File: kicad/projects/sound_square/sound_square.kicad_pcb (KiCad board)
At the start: 2 copper layers, 203.2 x 97.8 mm, 83 parts, among them J1 peripheral_addr_bus_connector, J2 peripheral_aux_connector, J3 peripheral_membank_connector, J4 Conn_01x06_Socket, J5 Conn_01x03_Pin, J7 Conn_02x05_Odd_Even, U1 74HC40103, U10 74HC08, U11 74HC32, U12 74HC02, U13 74HC08, U14 74HC40103, U15 74HC273, U16 74HC574, U17 74HC40103, U18 74HC157, U19 74HC157, U2 74HC40103, U20 74HC04, U21 74HC11, U22 74HC161, U23 74HC238, U24 74HC238, U3 74HC273, U4 74HC109, U5 74HC02, U6 74HC157, U7 74HC04, U8 74HC157, U9 74HC574, X1 CXO_DIP8

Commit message: Bit of noodling with sound square schem and PCB.
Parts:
- added C28: C, Capacitor_THT:C_Disc_D5.0mm_W2.5mm_P5.00mm, F.Cu at (157.5, 66.0)
- added C29: C, Capacitor_THT:C_Disc_D5.0mm_W2.5mm_P5.00mm, F.Cu at (200.7, 66.0)
- added J10: Conn_01x03_Socket, Connector_PinSocket_2.54mm:PinSocket_1x03_P2.54mm_Horizontal, F.Cu at (142.2, 61.0)
- added J11: Conn_01x04_Socket, Connector_PinSocket_2.54mm:PinSocket_1x04_P2.54mm_Horizontal, F.Cu at (165.1, 61.0)
- added J12: Stereo select B, Connector_PinHeader_2.54mm:PinHeader_2x02_P2.54mm_Vertical, F.Cu at (127.0, 57.1)
- added J13: Stereo select A, Connector_PinHeader_2.54mm:PinHeader_2x02_P2.54mm_Vertical, F.Cu at (168.9, 73.7)
- added J6: 10k R2R ladder, Connector_PinHeader_2.54mm:PinHeader_1x09_P2.54mm_Vertical, F.Cu at (137.2, 71.1)
- added J8: 10k R2R ladder, Connector_PinHeader_2.54mm:PinHeader_1x09_P2.54mm_Vertical, F.Cu at (177.8, 71.1)
- added J9: Conn_01x02_Pin, Connector_PinHeader_2.54mm:PinHeader_1x02_P2.54mm_Vertical, F.Cu at (203.2, 86.4)
- added R6: R_US, Resistor_THT:R_Axial_DIN0207_L6.3mm_D2.5mm_P10.16mm_Horizontal, F.Cu at (121.9, 66.0)
- added R7: R_US, Resistor_THT:R_Axial_DIN0207_L6.3mm_D2.5mm_P10.16mm_Horizontal, F.Cu at (147.3, 66.0)
- added R8: R_US, Resistor_THT:R_Axial_DIN0207_L6.3mm_D2.5mm_P10.16mm_Horizontal, F.Cu at (191.8, 66.0)
- added R9: R_US, Resistor_THT:R_Axial_DIN0207_L6.3mm_D2.5mm_P10.16mm_Horizontal, F.Cu at (179.1, 66.0)
- moved R4 19.8 mm to (217.2, 86.4), turned to 90 degrees
- moved U23 18.2 mm to (248.9, 77.5), turned to -90 degrees
- moved U24 18.2 mm to (104.1, 77.5), turned to -90 degrees
- moved R1 15.9 mm to (118.1, 71.1)
- moved J5 7.41 mm to (209.6, 86.4)
- moved C24 5.08 mm to (226.1, 82.5)
- moved C17 3.81 mm to (111.8, 77.5)
- moved C18 3.81 mm to (53.3, 77.5)
- moved C23 3.81 mm to (142.2, 82.5)
- moved C25 3.81 mm to (81.3, 82.5)
- moved C26 3.81 mm to (174.0, 82.5)
- moved J7 3.81 mm to (194.3, 76.2)
- moved U12 3.81 mm to (58.4, 85.1)
- moved U21 3.81 mm to (116.8, 85.1)
- moved U22 3.81 mm to (147.3, 85.1)
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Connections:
- U11 pad 10: /MIN_VOL_A -> /MIN_VOL_B
- U13 pad 8: /MIN_VOL_A -> /MIN_VOL_B
- U18 pad 1: /TOGGLE_OUT -> /TOGGLE_OUT_B
- U19 pad 1: /MIN_VOL_A -> /MIN_VOL_B
- U23 pad 1: unconnected-(U23-A0-Pad1) -> /VOL_A_3
- U23 pad 2: unconnected-(U23-A1-Pad2) -> /VOL_A_2
- U23 pad 3: unconnected-(U23-A2-Pad3) -> /VOL_A_1
- U24 pad 1: unconnected-(U24-A0-Pad1) -> /VOL_B_1
- U24 pad 2: unconnected-(U24-A1-Pad2) -> /VOL_B_2
- U24 pad 3: unconnected-(U24-A2-Pad3) -> /VOL_B_3

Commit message: Bit of work on BOM, bit of work on sound square.
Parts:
- removed C28, C29: C, Capacitor_THT:C_Disc_D5.0mm_W2.5mm_P5.00mm
- removed J10: Conn_01x03_Socket, Connector_PinSocket_2.54mm:PinSocket_1x03_P2.54mm_Horizontal
- removed J13: Stereo select A, Connector_PinHeader_2.54mm:PinHeader_2x02_P2.54mm_Vertical
- removed R7, R9: R_US, Resistor_THT:R_Axial_DIN0207_L6.3mm_D2.5mm_P10.16mm_Horizontal
- removed U21: 74HC11, Package_DIP:DIP-14_W7.62mm_Socket
- added C27: C, Capacitor_THT:C_Disc_D5.0mm_W2.5mm_P5.00mm, F.Cu at (172.7, 71.1)
- added R5: 100K, Resistor_THT:R_Axial_DIN0207_L6.3mm_D2.5mm_P10.16mm_Horizontal, F.Cu at (193.0, 71.1)
- added RV1: 100K, Potentiometer_THT:Potentiometer_Bourns_3386P_Vertical, F.Cu at (127.0, 61.0)
- added RV2: 100K, Potentiometer_THT:Potentiometer_Bourns_3386P_Vertical, F.Cu at (175.3, 61.0)
- added U25: LM358, Package_DIP:DIP-8_W7.62mm_Socket, F.Cu at (190.5, 66.0)
- added U26: 74HC10, Package_DIP:DIP-14_W7.62mm_Socket, F.Cu at (116.8, 85.1)
- J12: value Stereo select B -> Conn_01x02_Socket; footprint Connector_PinHeader_2.54mm:PinHeader_2x02_P2.54mm_Vertical -> Connector_PinSocket_2.54mm:PinSocket_1x02_P2.54mm_Horizontal
- R4: value 10K -> 100K
- R6, R8: value R_US -> 100K
- moved R6 84.0 mm to (205.7, 71.1)
- moved R4 82.5 mm to (137.2, 66.0), turned to 0 degrees
- moved J8 29.6 mm to (203.2, 86.4)
- moved R8 29.2 mm to (162.6, 66.0)
- moved U23 19.3 mm to (231.1, 85.1), turned to 90 degrees
- moved U24 19.3 mm to (86.4, 85.1), turned to 90 degrees
- moved J12 18.2 mm to (144.8, 61.0), turned to -90 degrees
- moved J7 16.5 mm to (177.8, 76.2)
- moved C26 14.4 mm to (182.9, 71.1), turned to 0 degrees
- moved J9 10.5 mm to (205.7, 76.2), turned to -90 degrees
- moved X1 8.89 mm to (188.0, 85.1)
- moved J5 5.24 mm to (208.3, 81.3), turned to -90 degrees
- turned C1 to 180 degrees
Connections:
- J11 pad 3: /OUT_R -> /AUDIO_OUT_UNBIASED
- J11 pad 4: /OUT_L -> /AUDIO_OUT_UNBIASED
- J12 pad 1: Net-(J12-Pin_1) -> /COMMON_AUDIO_BIASED
- J12 pad 2: /COMMON_L -> /EXT_CLK
- R4 pad 1: /DIVIDED_CLOCK -> /B_OUT_BIASED
- R4 pad 2: GND -> /COMMON_AUDIO_BIASED
- R6 pad 2: Net-(J12-Pin_3) -> VCC
- R8 pad 1: Net-(C29-Pad2) -> /A_OUT_BIASED
- R8 pad 2: Net-(J13-Pin_1) -> /COMMON_AUDIO_BIASED
- U12 pad 10: /~{CHANNEL_B_WRITE} -> unconnected-(U12-Pad10)
- U12 pad 8: /CHANNEL_B_WRITE -> GND
- U12 pad 9: /CHANNEL_B_WRITE -> GND
- U7 pad 12: /~{CHANNEL_A_WRITE} -> unconnected-(U7-Pad12)
- U7 pad 13: /CHANNEL_A_WRITE -> GND

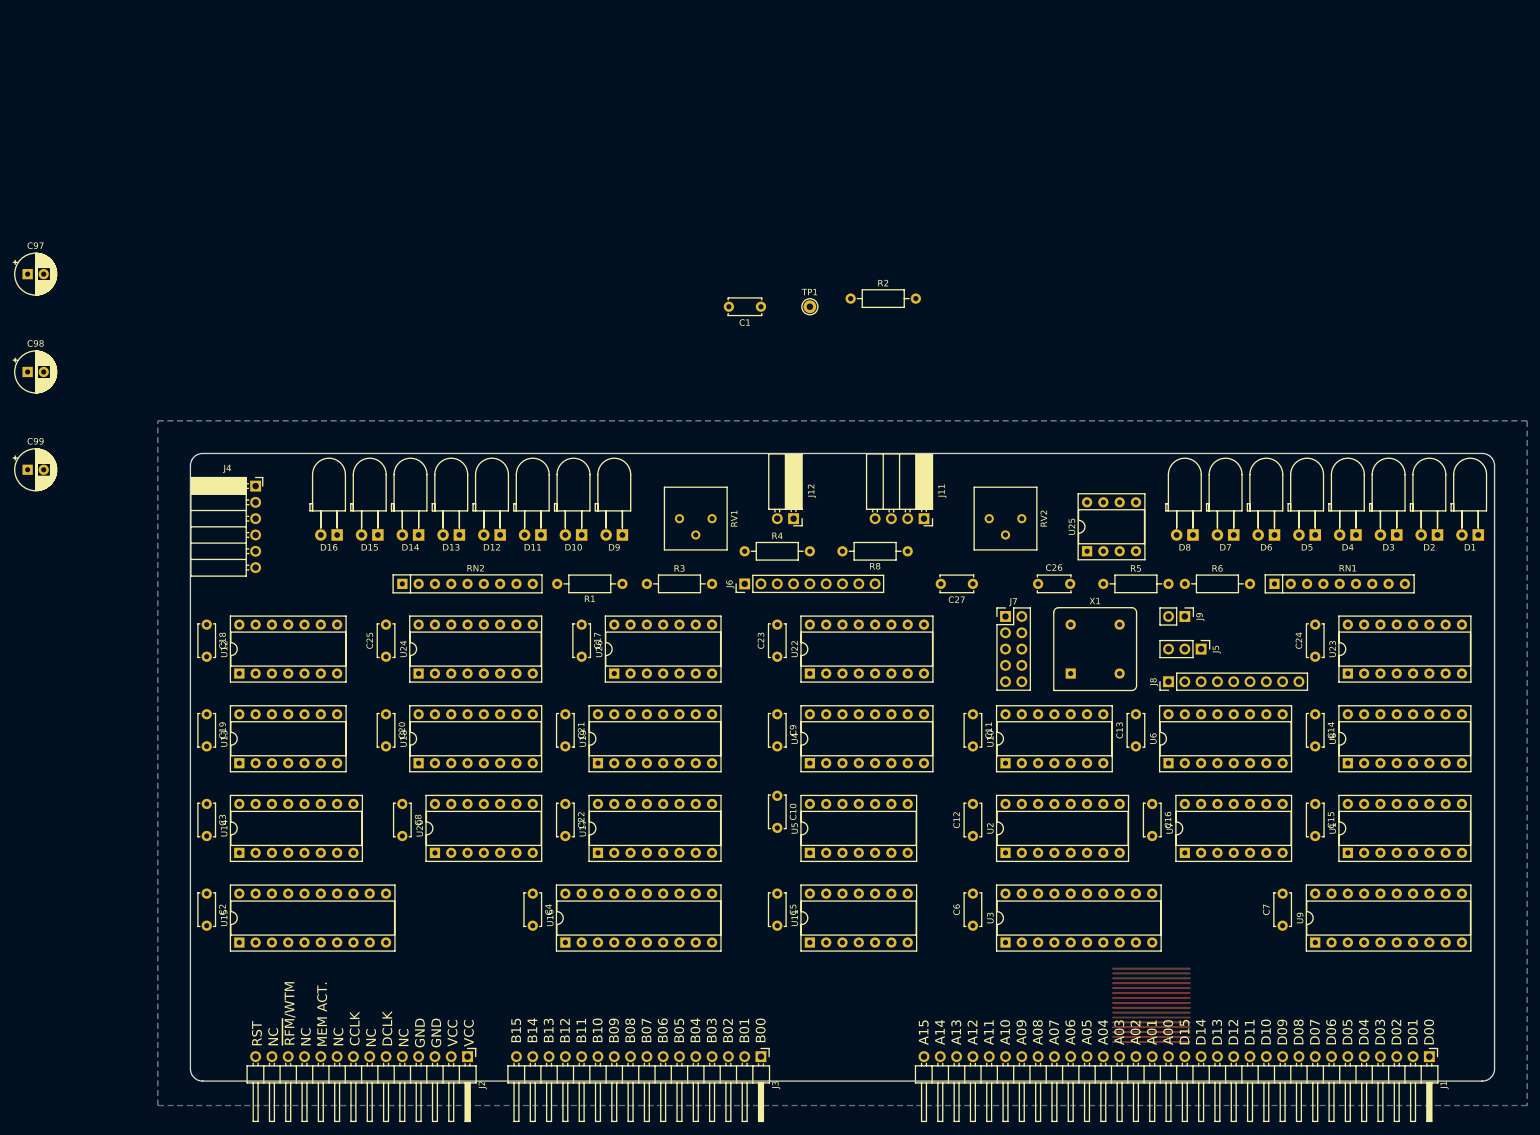
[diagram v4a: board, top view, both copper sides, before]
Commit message: Change NOR to OR for combining TCs of counters on sound square.
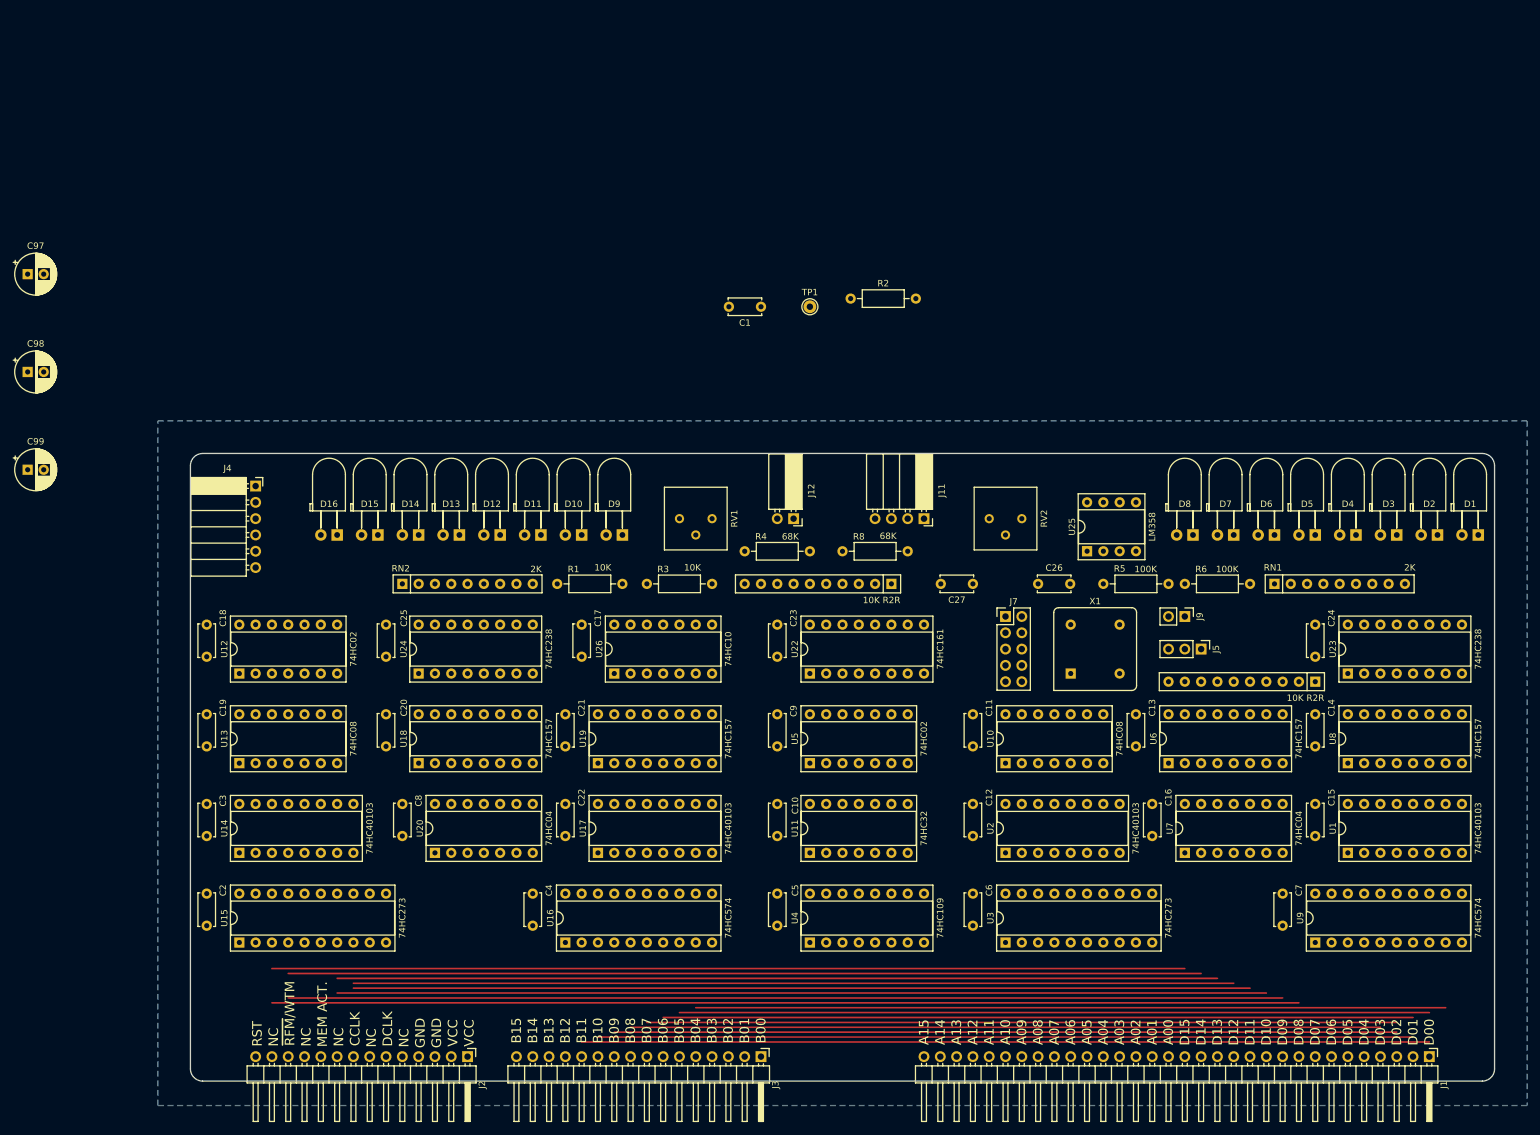
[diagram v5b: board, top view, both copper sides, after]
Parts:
- removed J6: 10k R2R ladder, Connector_PinHeader_2.54mm:PinHeader_1x09_P2.54mm_Vertical
- added J10: 10K R2R, Resistor_THT:R_Array_SIP10, F.Cu at (226.1, 86.4)
- C10, C11, C12, C13, C14, C15, C16, C17, C18, C19, C2, C20, C21, C22, C23, C24, C25, C26, C27, C3, C4, C5, C6, C7, C8, C9: value C -> 0.1uF
- C97, C98, C99: value C_Polarized -> 33uF
- J8: value 10k R2R ladder -> 10K R2R; footprint Connector_PinHeader_2.54mm:PinHeader_1x09_P2.54mm_Vertical -> Resistor_THT:R_Array_SIP10
- R4, R8: value 100K -> 68K
- RN1, RN2: value R_Network08_US -> 2K
- moved J8 45.8 mm to (160.0, 71.1), turned to 180 degrees
- moved U4 27.9 mm to (147.3, 127.0)
- moved U11 14.0 mm to (147.3, 113.0)
- moved U5 14.0 mm to (147.3, 99.1)
- moved C10 1.27 mm to (142.2, 105.4)
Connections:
- J8 pad 1: GND -> /B_OUT_BIASED
- J8 pad 2: /R2R_A_0 -> unconnected-(J8-Pin_2-Pad2)
- J8 pad 3: /R2R_A_1 -> unconnected-(J8-Pin_3-Pad3)
- J8 pad 4: /R2R_A_2 -> unconnected-(J8-Pin_4-Pad4)
- J8 pad 5: /R2R_A_3 -> /R2R_B_4
- J8 pad 6: /R2R_A_4 -> /R2R_B_3
- J8 pad 7: unconnected-(J8-Pin_7-Pad7) -> /R2R_B_2
- J8 pad 8: unconnected-(J8-Pin_8-Pad8) -> /R2R_B_1
- J8 pad 9: /A_OUT_BIASED -> /R2R_B_0
- U1 pad 15: Net-(U1-~{PE}) -> /~{ZERO_A}
- U11 pad 1: GND -> Net-(U1-~{TC})
- U11 pad 2: GND -> Net-(U2-~{TC})
- U11 pad 3: unconnected-(U11-Pad3) -> /~{ZERO_A}
- U11 pad 4: GND -> Net-(U14-~{TE})
- U11 pad 5: GND -> Net-(U14-~{TC})
- U11 pad 6: unconnected-(U11-Pad6) -> /~{ZERO_B}
- U14 pad 15: Net-(U14-~{PE}) -> /~{ZERO_B}
- U17 pad 15: Net-(U14-~{PE}) -> /~{ZERO_B}
- U2 pad 15: Net-(U1-~{PE}) -> /~{ZERO_A}
- U23 pad 1: /VOL_A_3 -> /VOL_A_1
- U23 pad 3: /VOL_A_1 -> /VOL_A_3
- U4 pad 12: Net-(U14-~{TC}) -> /~{ZERO_B}
- U4 pad 4: Net-(U2-~{TC}) -> /~{ZERO_A}
- U5 pad 10: Net-(U14-~{PE}) -> unconnected-(U5-Pad10)
- U5 pad 11: Net-(U1-~{TC}) -> GND
- U5 pad 12: Net-(U2-~{TC}) -> GND
- U5 pad 13: Net-(U1-~{PE}) -> unconnected-(U5-Pad13)
- U5 pad 8: Net-(U14-~{TE}) -> GND
- U5 pad 9: Net-(U14-~{TC}) -> GND
- U6 pad 1: /TOGGLE_OUT -> /TOGGLE_OUT_A
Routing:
- net (no net): track 191.0 -> 0.00 mm
- net /DATA_BUS_08: track 0.00 -> 160.0 mm
- net /DATA_BUS_09: track 0.00 -> 154.9 mm
- net /DATA_BUS_10: track 0.00 -> 144.8 mm
- net /DATA_BUS_15: track 0.00 -> 142.2 mm
- net /DATA_BUS_14: track 0.00 -> 142.2 mm
- net /DATA_BUS_11: track 0.00 -> 139.7 mm
- net /DATA_BUS_12: track 0.00 -> 137.2 mm
- net /DATA_BUS_13: track 0.00 -> 137.2 mm
- net /DATA_BUS_00: track 0.00 -> 132.1 mm
- net /DATA_BUS_01: track 0.00 -> 127.0 mm
- net /DATA_BUS_02: track 0.00 -> 121.9 mm
- net /DATA_BUS_05: track 0.00 -> 116.8 mm
- net /DATA_BUS_07: track 0.00 -> 116.8 mm
- net /DATA_BUS_06: track 0.00 -> 116.8 mm
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
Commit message: Start on sound square PCB.
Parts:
- moved C26 0.08 mm to (183.0, 71.1)
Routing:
- net VCC: track 0.00 -> 578.3 mm, vias 0 -> 4
- net /DATA_CLK: track 0.00 -> 247.1 mm, vias 0 -> 7
- net /CHOSEN_CLK: track 0.00 -> 159.0 mm, vias 0 -> 5
- net /~{RESET}: track 0.00 -> 124.0 mm, vias 0 -> 1
- net Net-(U14-~{TC}): track 0.00 -> 97.1 mm, vias 0 -> 6
- net Net-(U14-~{TE}): track 0.00 -> 59.8 mm, vias 0 -> 5
- net /SAFE_CLK_B: track 0.00 -> 59.4 mm, vias 0 -> 4
- net /TOGGLE_OUT_B: track 0.00 -> 58.7 mm, vias 0 -> 3
- net /VOL_B_3: track 0.00 -> 40.9 mm, vias 0 -> 1
- net /VOL_B_1: track 0.00 -> 39.4 mm, vias 0 -> 1
- net /VOL_B_2: track 0.00 -> 38.3 mm, vias 0 -> 1
- net /COUNT_B_7: track 0.00 -> 26.2 mm
- net /VOL_B_0: track 0.00 -> 25.3 mm
- net /COUNT_B_4: track 0.00 -> 23.8 mm
- net Net-(U12-Pad1): track 0.00 -> 20.5 mm
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
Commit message: More work on sound square PCB.
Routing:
- net /~{RFM}/WTM: track 0.00 -> 153.9 mm, vias 0 -> 8
- net /MEM_ACT: track 0.00 -> 153.7 mm, vias 0 -> 8
- net /~{ZERO_B}: track 0.00 -> 77.6 mm, vias 0 -> 4
- net /~{CHANNEL_B_WRITE}: track 0.00 -> 73.7 mm, vias 0 -> 4
- net /SAFE_CLK_B: track 59.4 -> 127.6 mm, vias 4 -> 7
- net /MIN_VOL_B: track 0.00 -> 67.0 mm, vias 0 -> 5
- net /~{DATA_CLK}: track 17.4 -> 84.1 mm, vias 0 -> 3
- net /~{VOL_B_0}: track 0.00 -> 63.7 mm, vias 0 -> 5
- net /~{VOL_B_2}: track 0.00 -> 58.1 mm, vias 0 -> 2
- net /~{VOL_B_1}: track 0.00 -> 56.6 mm, vias 0 -> 1
- net /RESET: track 0.00 -> 52.6 mm
- net Net-(D16-A): track 0.00 -> 45.9 mm, vias 0 -> 4
- net /~{VOL_B_3}: track 0.00 -> 45.6 mm, vias 0 -> 2
- net VCC: track 578.3 -> 620.7 mm
- net Net-(D15-A): track 0.00 -> 41.2 mm
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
